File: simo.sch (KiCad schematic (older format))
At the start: 15 parts, among them J1 PWR ENA_BAT, J10 Conn_01x10_Female, J11 Conn_01x16_Female, J12 Conn_01x14_Female, J13 Conn_01x16_Female, J14 Conn_01x10_Female, J2 SIM7000G_CMD, J3 Conector_Memoria_Flash_EXT, J4 Conn_01x04_Female, J5 Conn_01x02_Female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

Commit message: se termino template y huella  del modulo 4g sim7000g
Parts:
- J3: footprint Connector_Wago:Wago_734-136_1x06_P3.50mm_Vertical -> Connector_PinSocket_2.54mm:PinSocket_1x06_P2.54mm_Vertical
- J4: footprint Connector_Wago:Wago_734-134_1x04_P3.50mm_Vertical -> Connector_PinSocket_2.54mm:PinSocket_1x04_P2.54mm_Vertical
- J5, J6: footprint Connector_Wago:Wago_734-132_1x02_P3.50mm_Vertical -> Connector_PinSocket_2.54mm:PinSocket_1x02_P2.54mm_Vertical
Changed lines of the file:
@@
 F 0 "J3" H 842 2375 50  0000 C CNN
 F 1 "Conector_Memoria_Flash_EXT" H 842 2466 50  0000 C CNN
-F 2 "Connector_Wago:Wago_734-136_1x06_P3.50mm_Vertical" H 950 2900 50  0001 C CNN
+F 2 "Connector_PinSocket_2.54mm:PinSocket_1x06_P2.54mm_Vertical" H 950 2900 50  0001 C CNN
 F 3 "~" H 950 2900 50  0001 C CNN
 	1    950  2900
@@
 F 0 "J6" H 6328 2376 50  0000 L CNN
 F 1 "Conn_01x02_Female" H 6328 2285 50  0000 L CNN
-F 2 "Connector_Wago:Wago_734-132_1x02_P3.50mm_Vertical" H 6300 2400 50  0001 C CNN
+F 2 "Connector_PinSocket_2.54mm:PinSocket_1x02_P2.54mm_Vertical" H 6300 2400 50  0001 C CNN
 F 3 "~" H 6300 2400 50  0001 C CNN
 	1    6300 2400
@@
 F 0 "J4" V 3938 512 50  0000 R CNN
 F 1 "Conn_01x04_Female" V 3847 512 50  0000 R CNN
-F 2 "Connector_Wago:Wago_734-134_1x04_P3.50mm_Vertical" H 4000 800 50  0001 C CNN
+F 2 "Connector_PinSocket_2.54mm:PinSocket_1x04_P2.54mm_Vertical" H 4000 800 50  0001 C CNN
 F 3 "~" H 4000 800 50  0001 C CNN
 	1    4000 800
@@
 F 0 "J5" H 6328 1576 50  0000 L CNN
 F 1 "Conn_01x02_Female" H 6328 1485 50  0000 L CNN
-F 2 "Connector_Wago:Wago_734-132_1x02_P3.50mm_Vertical" H 6300 1600 50  0001 C CNN
+F 2 "Connector_PinSocket_2.54mm:PinSocket_1x02_P2.54mm_Vertical" H 6300 1600 50  0001 C CNN
 F 3 "~" H 6300 1600 50  0001 C CNN
 	1    6300 1600

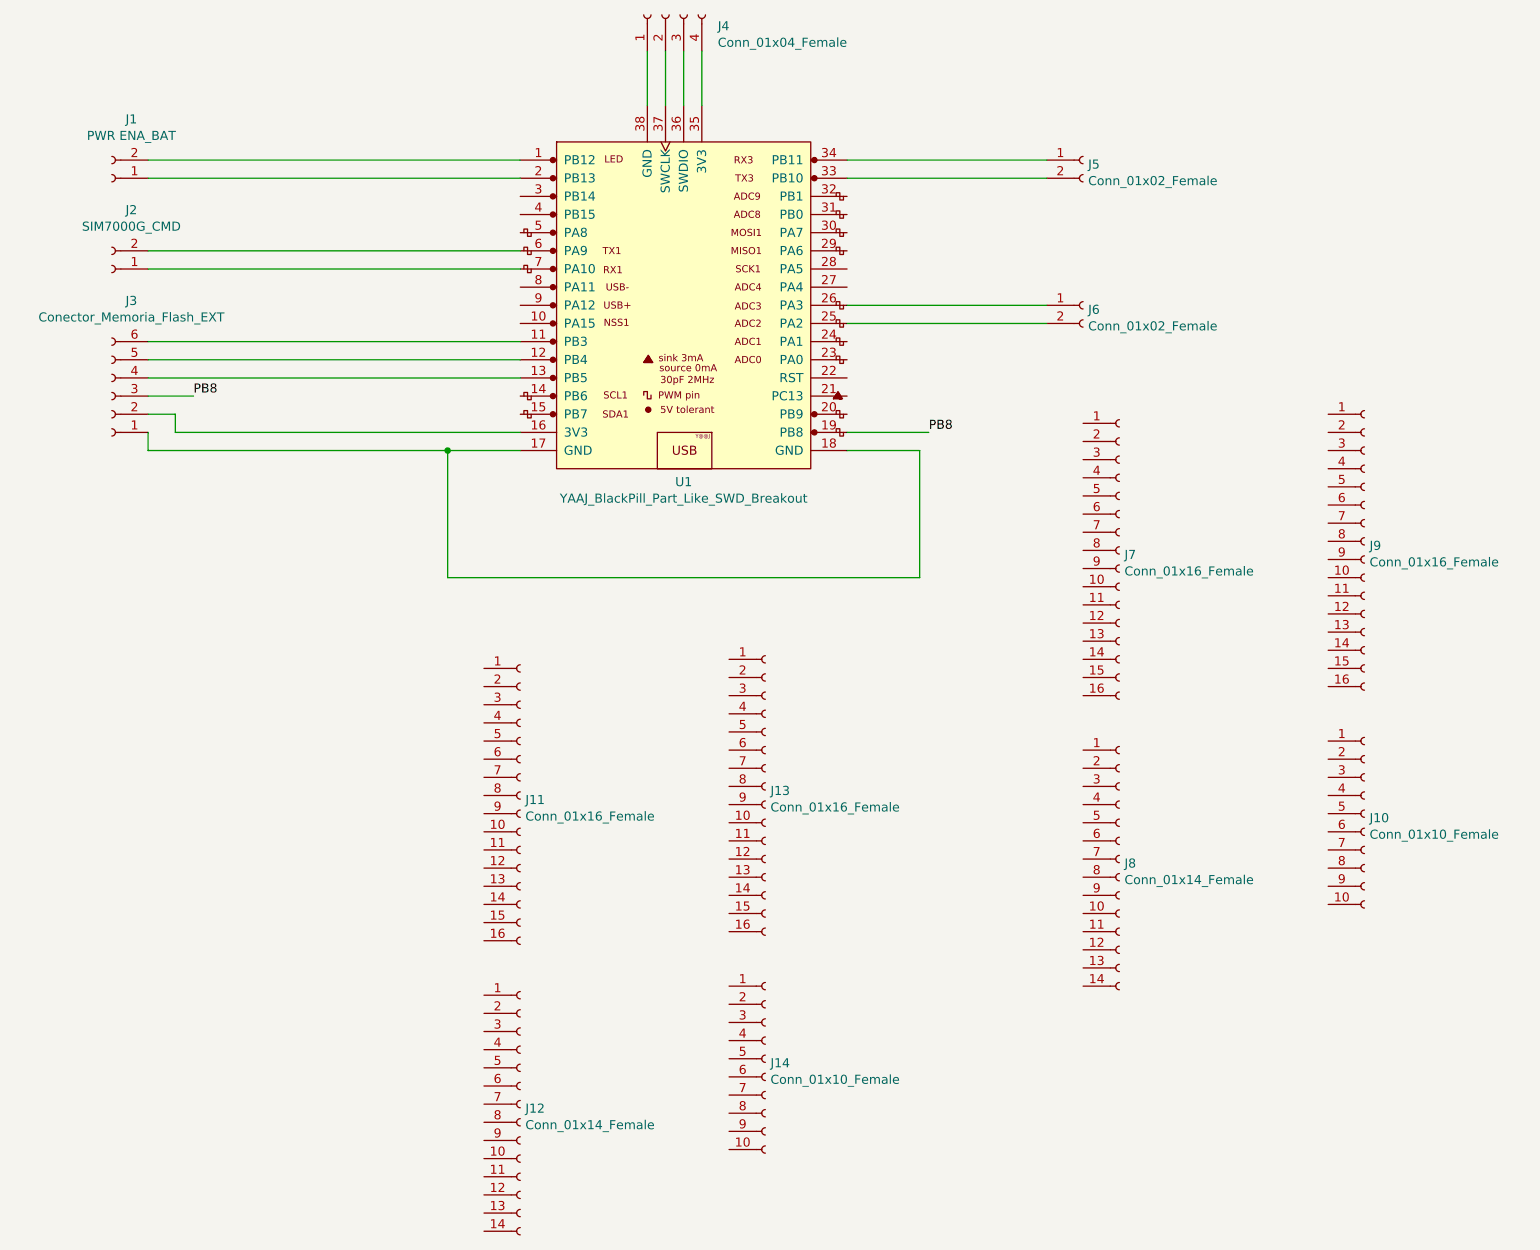
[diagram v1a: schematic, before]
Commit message: se agregaron huellas de : memoria flash ext, debug_usb y conversor_dc_dc
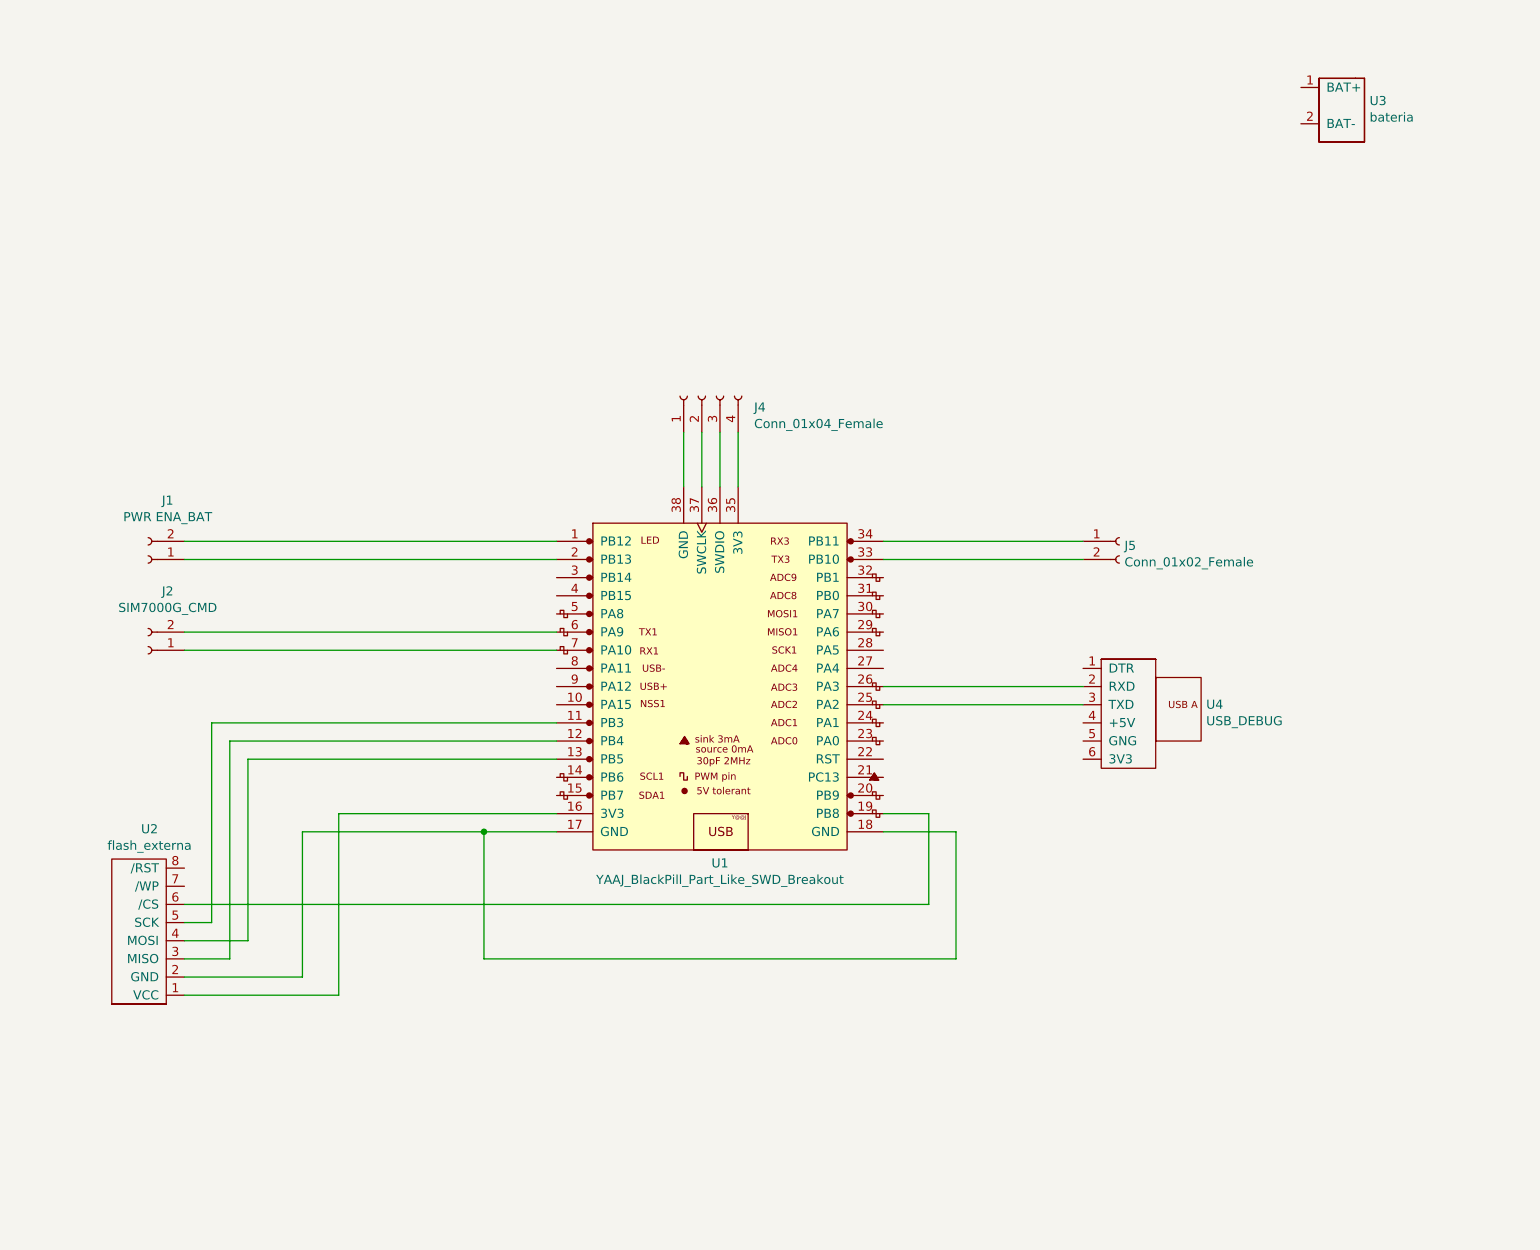
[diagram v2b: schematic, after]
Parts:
- removed J10, J14: Conn_01x10_Female, Connector_PinSocket_2.54mm:PinSocket_1x10_P2.54mm_Vertical, symbol Connector:Conn_01x10_Female
- removed J11, J13, J7, J9: Conn_01x16_Female, Connector_PinSocket_2.54mm:PinSocket_1x16_P2.54mm_Vertical, symbol Connector:Conn_01x16_Female
- removed J12, J8: Conn_01x14_Female, Connector_PinSocket_2.54mm:PinSocket_1x14_P2.54mm_Vertical, symbol Connector:Conn_01x14_Female
- removed J3: Conector_Memoria_Flash_EXT, Connector_PinSocket_2.54mm:PinSocket_1x06_P2.54mm_Vertical, symbol Connector:Conn_01x06_Female
- removed J6: Conn_01x02_Female, Connector_PinSocket_2.54mm:PinSocket_1x02_P2.54mm_Vertical, symbol Connector:Conn_01x02_Female
- added U2: flash_externa, bluepill:conector_flash_ext, symbol YAAJ_BlackPill:flash_externa
- added U3: bateria, bluepill:bateria, symbol YAAJ_BlackPill:bateria
- added U4: USB_DEBUG, bluepill:debug_usb, symbol YAAJ_BlackPill:USB_DEBUG
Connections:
- net at U1.11 (PB3): now also U2.5 (SCK)
- net at U1.12 (PB4): now also U2.3 (MISO)
- net at U1.13 (PB5): now also U2.4 (MOSI)
- net at U1.16 (3V3): now also U2.1 (VCC)
- net at U1.17 (GND), U1.18 (GND): now also U2.2 (GND)
- net at U1.25 (PA2): now also U4.3 (TXD)
- net at U1.26 (PA3): now also U4.2 (RXD)
- net PB8: no longer names the net of U1.19 (PB8)
- net PB8: now also U2.6 (/CS)
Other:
- moved on the sheet: J1, J2, J4, J5, U1
